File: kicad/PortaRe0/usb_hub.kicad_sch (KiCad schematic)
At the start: 74 parts, among them U10 TPS2042BDR, U12 HC-USB3.0-L168-WP, U4 VL812, U5 W25Q32JVSSIQ, U7 TPS61023DRLR, U8 USB31-TYPE-C-FSABC, Y1 C9006

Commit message: Docs: session34終了処理・0402化確定・ディスプレイ調査・PCBレイアウト進行中
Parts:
- C100, C101, C103, C105, C106, C111, C112, C14, C15, C16, C17, C18, C19, C20, C22, C23, C24, C25, C26, C28, C30, C32, C34, C36, C38, C41, C42, C44, C46, C47, C48, C52, C53, C58, C59, C66, C67: footprint Capacitor_SMD:C_0603_1608Metric -> Capacitor_SMD:C_0402_1005Metric
- R12, R13, R15, R16, R17, R19, R20, R22, R23, R24, R25, R42, R43, R44, R46, R47, R58, R59: footprint Resistor_SMD:R_0603_1608Metric -> Resistor_SMD:R_0402_1005Metric
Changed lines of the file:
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@@
 			)
 		)
-		(property "Footprint" "Capacitor_SMD:C_0603_1608Metric"
+		(property "Footprint" "Capacitor_SMD:C_0402_1005Metric"
 			(at 35.56 139.7 0)
 			(effects
@@
 			)
 		)
-		(property "Footprint" "Capacitor_SMD:C_0603_1608Metric"
+		(property "Footprint" "Capacitor_SMD:C_0402_1005Metric"
 			(at 138.43 111.76 0)
 			(effects
@@
 			)
 		)
-		(property "Footprint" "Capacitor_SMD:C_0603_1608Metric"
+		(property "Footprint" "Capacitor_SMD:C_0402_1005Metric"
 			(at 128.27 261.62 0)
 			(effects
@@
 			)
 		)
-		(property "Footprint" "Capacitor_SMD:C_0603_1608Metric"
+		(property "Footprint" "Capacitor_SMD:C_0402_1005Metric"
 			(at 148.59 68.58 0)
 			(effects
@@
 			)
 		)
-		(property "Footprint" "Capacitor_SMD:C_0603_1608Metric"
+		(property "Footprint" "Capacitor_SMD:C_0402_1005Metric"
 			(at 55.88 132.08 0)
 			(effects
@@
 			)
 		)
-		(property "Footprint" "Capacitor_SMD:C_0603_1608Metric"
+		(property "Footprint" "Capacitor_SMD:C_0402_1005Metric"
 			(at 101.6 106.68 0)
 			(effects
@@
 			)
 		)
-		(property "Footprint" "Capacitor_SMD:C_0603_1608Metric"
+		(property "Footprint" "Capacitor_SMD:C_0402_1005Metric"
 			(at 123.19 55.88 0)
 			(effects
@@
 			)
 		)
-		(property "Footprint" "Capacitor_SMD:C_0603_1608Metric"
+		(property "Footprint" "Capacitor_SMD:C_0402_1005Metric"
 			(at 160.02 201.93 0)
 			(effects
@@
 			)
 		)
-		(property "Footprint" "Resistor_SMD:R_0603_1608Metric"
+		(property "Footprint" "Resistor_SMD:R_0402_1005Metric"
 			(at 180.34 157.48 0)
 			(effects
@@
 			)
 		)
-		(property "Footprint" "Capacitor_SMD:C_0603_1608Metric"
+		(property "Footprint" "Capacitor_SMD:C_0402_1005Metric"
 			(at 67.31 147.32 0)
 			(effects
@@
 			)
 		)
-		(property "Footprint" "Resistor_SMD:R_0603_1608Metric"
+		(property "Footprint" "Resistor_SMD:R_0402_1005Metric"
 			(at 194.31 142.24 0)
 			(effects
@@
 			)
 		)
-		(property "Footprint" "Resistor_SMD:R_0603_1608Metric"
+		(property "Footprint" "Resistor_SMD:R_0402_1005Metric"
 			(at 401.32 43.18 0)
 			(effects
@@
 			)
 		)
-		(property "Footprint" "Capacitor_SMD:C_0603_1608Metric"
+		(property "Footprint" "Capacitor_SMD:C_0402_1005Metric"
 			(at 115.57 80.01 0)
 			(effects
@@
 			)
 		)
-		(property "Footprint" "Capacitor_SMD:C_0603_1608Metric"
+		(property "Footprint" "Capacitor_SMD:C_0402_1005Metric"
 			(at 111.76 212.09 0)
 			(effects
@@
 			)
 		)
-		(property "Footprint" "Resistor_SMD:R_0603_1608Metric"
+		(property "Footprint" "Resistor_SMD:R_0402_1005Metric"
 			(at 179.07 149.86 0)
 			(effects
@@
 			)
 		)
-		(property "Footprint" "Capacitor_SMD:C_0603_1608Metric"
+		(property "Footprint" "Capacitor_SMD:C_0402_1005Metric"
 			(at 111.76 201.93 0)
 			(effects
@@
 			)
 		)
-		(property "Footprint" "Capacitor_SMD:C_0603_1608Metric"
+		(property "Footprint" "Capacitor_SMD:C_0402_1005Metric"
 			(at 217.17 149.86 0)
 			(effects
@@
 			)
 		)
-		(property "Footprint" "Resistor_SMD:R_0603_1608Metric"
+		(property "Footprint" "Resistor_SMD:R_0402_1005Metric"
 			(at 179.07 134.62 0)
 			(effects
@@
 			)
 		)
-		(property "Footprint" "Capacitor_SMD:C_0603_1608Metric"
+		(property "Footprint" "Capacitor_SMD:C_0402_1005Metric"
 			(at 320.04 102.87 0)
 			(effects
@@
 			)
 		)
-		(property "Footprint" "Resistor_SMD:R_0603_1608Metric"
+		(property "Footprint" "Resistor_SMD:R_0402_1005Metric"
 			(at 208.28 139.7 0)
 			(effects
@@
 			)
 		)
-		(property "Footprint" "Capacitor_SMD:C_0603_1608Metric"
+		(property "Footprint" "Capacitor_SMD:C_0402_1005Metric"
 			(at 142.24 256.54 0)
 			(effects
@@
 			)
 		)
-		(property "Footprint" "Resistor_SMD:R_0603_1608Metric"
+		(property "Footprint" "Resistor_SMD:R_0402_1005Metric"
 			(at 297.18 38.1 0)
 			(effects
@@
 			)
 		)
-		(property "Footprint" "Resistor_SMD:R_0603_1608Metric"
+		(property "Footprint" "Resistor_SMD:R_0402_1005Metric"
 			(at 179.07 137.16 0)
 			(effects
@@
 			)
 		)
-		(property "Footprint" "Resistor_SMD:R_0603_1608Metric"
+		(property "Footprint" "Resistor_SMD:R_0402_1005Metric"
 			(at 140.97 212.09 0)
 			(effects
@@
 			)
 		)
-		(property "Footprint" "Capacitor_SMD:C_0603_1608Metric"
+		(property "Footprint" "Capacitor_SMD:C_0402_1005Metric"
 			(at 382.27 38.1 0)
 			(effects
@@
 			)
 		)
-		(property "Footprint" "Capacitor_SMD:C_0603_1608Metric"
+		(property "Footprint" "Capacitor_SMD:C_0402_1005Metric"
 			(at 35.56 172.72 0)
 			(effects
@@
 			)
 		)
-		(property "Footprint" "Resistor_SMD:R_0603_1608Metric"
+		(property "Footprint" "Resistor_SMD:R_0402_1005Metric"
 			(at 199.39 165.1 0)
 			(effects
@@
 			)
 		)
-		(property "Footprint" "Capacitor_SMD:C_0603_1608Metric"
+		(property "Footprint" "Capacitor_SMD:C_0402_1005Metric"
 			(at 299.72 130.81 0)
 			(effects
@@
 			)
 		)
-		(property "Footprint" "Resistor_SMD:R_0603_1608Metric"
+		(property "Footprint" "Resistor_SMD:R_0402_1005Metric"
 			(at 199.39 162.56 0)
 			(effects
@@
 			)
 		)
-		(property "Footprint" "Resistor_SMD:R_0603_1608Metric"
+		(property "Footprint" "Resistor_SMD:R_0402_1005Metric"
 			(at 321.31 45.72 0)
 			(effects
@@
 			)
 		)
-		(property "Footprint" "Capacitor_SMD:C_0603_1608Metric"
+		(property "Footprint" "Capacitor_SMD:C_0402_1005Metric"
 			(at 162.56 91.44 0)
 			(effects
@@
 			)
 		)
-		(property "Footprint" "Capacitor_SMD:C_0603_1608Metric"
+		(property "Footprint" "Capacitor_SMD:C_0402_1005Metric"
 			(at 101.6 97.79 0)
 			(effects
@@
 			)
 		)
-		(property "Footprint" "Capacitor_SMD:C_0603_1608Metric"
+		(property "Footprint" "Capacitor_SMD:C_0402_1005Metric"
 			(at 130.81 31.75 0)
 			(effects
@@
 			)
 		)
-		(property "Footprint" "Capacitor_SMD:C_0603_1608Metric"
+		(property "Footprint" "Capacitor_SMD:C_0402_1005Metric"
 			(at 243.84 170.18 0)
 			(effects
@@
 			)
 		)
-		(property "Footprint" "Resistor_SMD:R_0603_1608Metric"
+		(property "Footprint" "Resistor_SMD:R_0402_1005Metric"
 			(at 189.23 144.78 0)
 			(effects
@@
 			)
 		)
-		(property "Footprint" "Capacitor_SMD:C_0603_1608Metric"
+		(property "Footprint" "Capacitor_SMD:C_0402_1005Metric"
 			(at 214.63 130.81 0)
 			(effects
@@
 			)
 		)
-		(property "Footprint" "Capacitor_SMD:C_0603_1608Metric"
+		(property "Footprint" "Capacitor_SMD:C_0402_1005Metric"
 			(at 245.11 151.13 0)
 			(effects
@@
 			)
 		)
-		(property "Footprint" "Resistor_SMD:R_0603_1608Metric"
+		(property "Footprint" "Resistor_SMD:R_0402_1005Metric"
 			(at 205.74 124.46 0)
 			(effects
@@
 			)
 		)
-		(property "Footprint" "Capacitor_SMD:C_0603_1608Metric"
+		(property "Footprint" "Capacitor_SMD:C_0402_1005Metric"
 			(at 118.11 198.12 0)
 			(effects
@@
 			)
 		)
-		(property "Footprint" "Capacitor_SMD:C_0603_1608Metric"
+		(property "Footprint" "Capacitor_SMD:C_0402_1005Metric"
 			(at 153.67 111.76 0)
 			(effects
@@
 			)
 		)
-		(property "Footprint" "Resistor_SMD:R_0603_1608Metric"
+		(property "Footprint" "Resistor_SMD:R_0402_1005Metric"
 			(at 297.18 93.98 0)
 			(effects
@@
 			)
 		)
-		(property "Footprint" "Resistor_SMD:R_0603_1608Metric"
+		(property "Footprint" "Resistor_SMD:R_0402_1005Metric"
 			(at 307.34 88.9 0)
 			(effects
@@
 			)
 		)
-		(property "Footprint" "Capacitor_SMD:C_0603_1608Metric"
+		(property "Footprint" "Capacitor_SMD:C_0402_1005Metric"
 			(at 160.02 212.09 0)
 			(effects
@@
 			)
 		)
-		(property "Footprint" "Resistor_SMD:R_0603_1608Metric"
+		(property "Footprint" "Resistor_SMD:R_0402_1005Metric"
 			(at 184.15 147.32 0)
 			(effects
@@
 			)
 		)
-		(property "Footprint" "Capacitor_SMD:C_0603_1608Metric"
+		(property "Footprint" "Capacitor_SMD:C_0402_1005Metric"
 			(at 135.89 111.76 0)
 			(effects
@@
 			)
 		)
-		(property "Footprint" "Capacitor_SMD:C_0603_1608Metric"
+		(property "Footprint" "Capacitor_SMD:C_0402_1005Metric"
 			(at 142.24 246.38 0)
 			(effects
@@
 			)
 		)
-		(property "Footprint" "Capacitor_SMD:C_0603_1608Metric"
+		(property "Footprint" "Capacitor_SMD:C_0402_1005Metric"
 			(at 35.56 160.02 0)
 			(effects
@@
 			)
 		)
-		(property "Footprint" "Capacitor_SMD:C_0603_1608Metric"
+		(property "Footprint" "Capacitor_SMD:C_0402_1005Metric"
 			(at 363.22 88.9 0)
 			(effects
@@
 			)
 		)
-		(property "Footprint" "Capacitor_SMD:C_0603_1608Metric"
+		(property "Footprint" "Capacitor_SMD:C_0402_1005Metric"
 			(at 120.65 198.12 0)
 			(effects
@@
 			)
 		)
-		(property "Footprint" "Resistor_SMD:R_0603_1608Metric"
+		(property "Footprint" "Resistor_SMD:R_0402_1005Metric"
 			(at 144.78 212.09 0)
 			(effects
@@
 			)
 		)
-		(property "Footprint" "Capacitor_SMD:C_0603_1608Metric"
+		(property "Footprint" "Capacitor_SMD:C_0402_1005Metric"
 			(at 46.99 172.72 0)
 			(effects
@@
 			)
 		)
-		(property "Footprint" "Capacitor_SMD:C_0603_1608Metric"
+		(property "Footprint" "Capacitor_SMD:C_0402_1005Metric"
 			(at 156.21 233.68 0)
 			(effects
@@
 			)
 		)
-		(property "Footprint" "Capacitor_SMD:C_0603_1608Metric"
+		(property "Footprint" "Capacitor_SMD:C_0402_1005Metric"
 			(at 234.95 151.13 0)
 			(effects
@@
 			)
 		)
-		(property "Footprint" "Capacitor_SMD:C_0603_1608Metric"
+		(property "Footprint" "Capacitor_SMD:C_0402_1005Metric"
 			(at 120.65 242.57 0)
 			(effects
@@
 			)
 		)
-		(property "Footprint" "Capacitor_SMD:C_0603_1608Metric"
+		(property "Footprint" "Capacitor_SMD:C_0402_1005Metric"
 			(at 156.21 111.76 0)
 			(effects

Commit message: Docs: session35終了処理・TPS61023 FB接続ミス確認・M.2クリアランス1.1mm
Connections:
- net 5V_SYS: no longer R45.1
- net HUB_5V: now also R45.1
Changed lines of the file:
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@@
 		)
 	)
+	(label "HUB_5V"
+		(at 318.77 86.36 0)
+		(effects
+			(font
+				(size 1.27 1.27)
+			)
+			(justify left bottom)
+		)
+	)
 	(label "USB1_VBUS"
 		(at 383.54 135.89 0)
@@
 					(unit 1)
 				)
-			)
-		)
-	)
-	(symbol
-		(lib_id "power:5V_SYS")
-		(at 318.77 86.36 0)
-		(unit 1)
-		(exclude_from_sim no)
-		(in_bom yes)
-		(on_board yes)
-		(dnp no)
-		(fields_autoplaced yes)
-		(property "Reference" "#PWR0174"
-			(at 318.77 90.17 0)
-			(effects
-				(font
-					(size 1.27 1.27)
-				)
-				(hide yes)
-			)
-		)
-		(property "Value" "5V_SYS"
-			(at 318.77 81.28 0)
-			(effects
-				(font
-					(size 1.27 1.27)
-				)
-			)
-		)
-		(property "Footprint" ""
-			(at 318.77 86.36 0)
-			(effects
-				(font
-					(size 1.27 1.27)
-				)
-				(hide yes)
-			)
-		)
-		(property "Datasheet" ""
-			(at 318.77 86.36 0)
-			(effects
-				(font
-					(size 1.27 1.27)
-				)
-				(hide yes)
-			)
-		)
-		(property "Description" "Power symbol creates a global label with name \"VSYS\""
-			(at 318.516 80.264 0)
-			(effects
-				(font
-					(size 1.27 1.27)
-				)
-				(hide yes)
-			)
-		)
-		(pin "1"
-		)
-		(instances
-			(project "PortaRe0"
-				(path "/479aadc4-f9a0-4ec2-b000-6a17237038f1/8e76808d-de08-4fd1-9155-9dd498f0d9f9"
-					(reference "#PWR0174")
-					(unit 1)
-				)

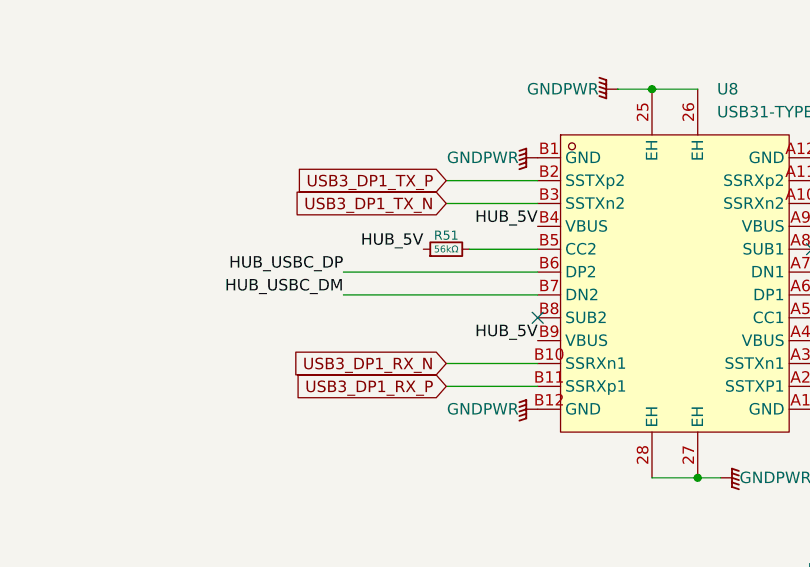
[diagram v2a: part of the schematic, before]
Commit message: Docs: session38終了処理・ルーティング大幅進捗（電源幹線〜USB差動ペア完了）
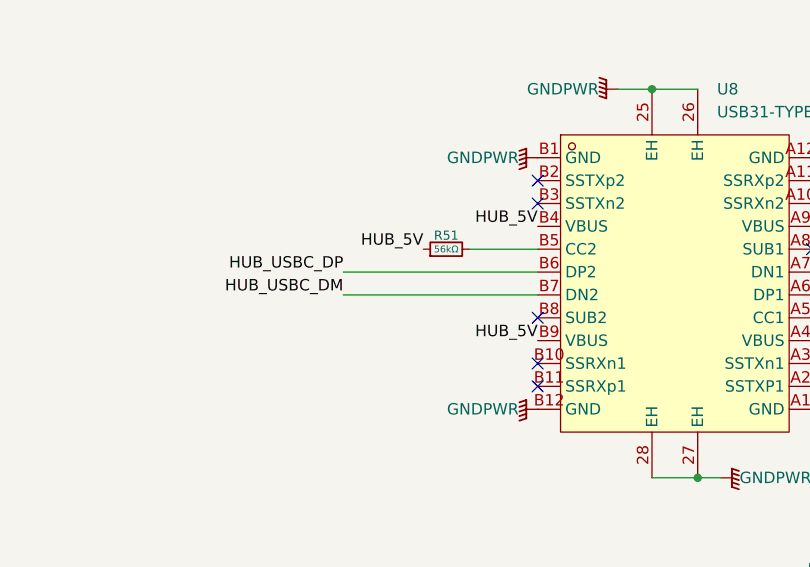
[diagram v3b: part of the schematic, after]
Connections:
- net USB3_DP1_RX_N: no longer U8.B10 (SSRXn1)
- net USB3_DP1_RX_P: no longer U8.B11 (SSRXp1)
- net USB3_DP1_TX_N: no longer U8.B3 (SSTXn2)
- net USB3_DP1_TX_P: no longer U8.B2 (SSTXp2)
- no-connect marks 11 -> 15
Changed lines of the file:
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@@
+	)
+	(no_connect
+		(at 275.59 275.59)
 	)
 	(no_connect
@@
 	)
 	(no_connect
+		(at 275.59 273.05)
+	)
+	(no_connect
+		(at 275.59 252.73)
+	)
+	(no_connect
 		(at 95.25 167.64)
 	)
@@
 	)
 	(no_connect
+		(at 275.59 255.27)
+	)
+	(no_connect
 		(at 95.25 144.78)
 	)
@@
 	(wire
 		(pts
-			(xy 265.43 275.59) (xy 275.59 275.59)
-		)
-		(stroke
-			(width 0)
-			(type default)
-		)
-	)
-	(wire
-		(pts
 			(xy 140.97 208.28) (xy 144.78 208.28)
 		)
@@
 	(wire
 		(pts
-			(xy 265.43 273.05) (xy 275.59 273.05)
-		)
-		(stroke
-			(width 0)
-			(type default)
-		)
-	)
-	(wire
-		(pts
 			(xy 205.74 133.35) (xy 205.74 139.7)
 		)
@@
 	(wire
 		(pts
-			(xy 265.43 255.27) (xy 275.59 255.27)
-		)
-		(stroke
-			(width 0)
-			(type default)
-		)
-	)
-	(wire
-		(pts
 			(xy 115.57 97.79) (xy 115.57 114.3)
 		)
@@
 		(pts
 			(xy 151.13 68.58) (xy 151.13 114.3)
-		)
-		(stroke
-			(width 0)
-			(type default)
-		)
-	)
-	(wire
-		(pts
-			(xy 265.43 252.73) (xy 275.59 252.73)
 		)
 		(stroke
@@
 		)
 	)
-	(global_label "USB3_DP1_RX_P"
-		(shape input)
-		(at 265.43 275.59 180)
-		(fields_autoplaced yes)
-		(effects
-			(font
-				(size 1.27 1.27)
-			)
-			(justify right)
-		)
-		(property "Intersheetrefs" "${INTERSHEET_REFS}"
-			(at 247.0235 275.59 0)
-			(effects
-				(font
-					(size 1.27 1.27)
-				)
-				(justify right)
-				(hide yes)
-			)
-		)
-	)
 	(global_label "USB3_DP2_RX_P"
 		(shape input)
@@
 		)
 	)
-	(global_label "USB3_DP1_TX_N"
-		(shape input)
-		(at 265.43 255.27 180)
-		(fields_autoplaced yes)
-		(effects
-			(font
-				(size 1.27 1.27)
-			)
-			(justify right)
-		)
-		(property "Intersheetrefs" "${INTERSHEET_REFS}"
-			(at 247.2654 255.27 0)
-			(effects
-				(font
-					(size 1.27 1.27)
-				)
-				(justify right)
-				(hide yes)
-			)
-		)
-	)
 	(global_label "USB3_DP1_TX_P"
 		(shape input)
@@
 	(global_label "USB3_DP1_TX_P"
 		(shape input)
-		(at 265.43 252.73 180)
-		(fields_autoplaced yes)
-		(effects
-			(font
-				(size 1.27 1.27)
-			)
-			(justify right)
-		)
-		(property "Intersheetrefs" "${INTERSHEET_REFS}"
-			(at 247.3259 252.73 0)
-			(effects
-				(font
-					(size 1.27 1.27)
-				)
-				(justify right)
-				(hide yes)
-			)
-		)
-	)
-	(global_label "USB3_DP1_TX_P"
-		(shape input)
 		(at 156.21 109.22 90)
 		(fields_autoplaced yes)
@@
 				(hide yes)
 			)
-		)
-	)
-	(global_label "USB3_DP1_RX_N"
-		(shape input)
-		(at 265.43 273.05 180)
-		(fields_autoplaced yes)
-		(effects
-			(font
-				(size 1.27 1.27)
-			)
-			(justify right)
-		)
-		(property "Intersheetrefs" "${INTERSHEET_REFS}"
-			(at 246.963 273.05 0)
-			(effects
-				(font
-					(size 1.27 1.27)
-				)
-				(justify right)
-				(hide yes)
-			)
